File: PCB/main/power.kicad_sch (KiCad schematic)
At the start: 32 parts, among them IC4 FT230XS-R, IC5 MCP73831T-2ACI_OT, IC6 MCP1700T-3302E_TT, J10 PZ254V-11-02P, J5 47346-0001, J6 PZ254V-11-02P, J7 PZ254V-11-02P, J8 MTP125-1103S1, Q1 IRF9540NPbF

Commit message: new PCB
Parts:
- IC4: footprint SOP64P599X175-16N -> SamacSys_Parts_Power:SOP64P599X175-16N
- IC5: footprint SOT95P270X145-5N -> SamacSys_Parts_Power:SOT95P270X145-5N
- IC6: footprint SOT95P237X112-3N -> SamacSys_Parts_Power:SOT95P237X112-3N
- J10: footprint HDRV2W64P0X254_1X2_508X250X873P -> SamacSys_Parts_Power:HDRV2W64P0X254_1X2_508X250X873P
- J5: footprint SamacSys_Parts_Power:47346-0001 -> SamacSys_Parts_Microcontroller:47346-0001
- J6, J7: footprint SamacSys_Parts:HDRV2W64P0X254_1X2_508X250X873P -> SamacSys_Parts_Power:HDRV2W64P0X254_1X2_508X250X873P
- J8: footprint SamacSys_Parts:HDRV3W64P0X254_1X3_762X250X885P -> SamacSys_Parts_Power:HDRV3W64P0X254_1X3_762X250X885P
- TP1, TP2, TP3, TP4: footprint SamacSys_Parts:5017 -> SamacSys_Parts_Power:5017
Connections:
- net USART1_TX renamed PA9
- net USATR1_RX renamed PA10
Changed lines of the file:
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@@
+    (stroke (width 0) (type default) (color 0 0 0 0))
+  )
+  (wire (pts (xy 111.76 149.86) (xy 116.84 149.86))
     (stroke (width 0) (type default) (color 0 0 0 0))
   )
@@
   )
   (wire (pts (xy 175.26 161.29) (xy 175.26 163.83))
+    (stroke (width 0) (type default) (color 0 0 0 0))
+  )
+  (wire (pts (xy 111.76 157.48) (xy 116.84 157.48))
     (stroke (width 0) (type default) (color 0 0 0 0))
   )
@@
     (effects (font (size 1.27 1.27)) (justify left bottom))
   )
-  (label "RXD" (at 116.84 157.48 0)
+  (label "RXD" (at 111.76 157.48 0)
     (effects (font (size 1.27 1.27)) (justify left bottom))
   )
@@
     (effects (font (size 1.27 1.27)) (justify left bottom))
   )
-  (label "TXD" (at 116.84 149.86 0)
+  (label "TXD" (at 111.76 149.86 0)
     (effects (font (size 1.27 1.27)) (justify left bottom))
   )
+  (label "PA10" (at 172.72 144.78 0)
+    (effects (font (size 1.27 1.27)) (justify left bottom))
+  )
   (label "D-" (at 110.49 71.12 0)
+    (effects (font (size 1.27 1.27)) (justify left bottom))
+  )
+  (label "PA9" (at 172.72 142.24 0)
     (effects (font (size 1.27 1.27)) (justify left bottom))
   )
@@
     )
   )
-  (global_label "USART1_TX" (shape input) (at 172.72 142.24 0) (fields_autoplaced)
-    (effects (font (size 1.27 1.27)) (justify left))
-    (property "Intersheet References" "${INTERSHEET_REFS}" (id 0) (at 185.2647 142.1606 0)
-      (effects (font (size 1.27 1.27)) (justify left) hide)
-    )
-  )
   (global_label "VCC" (shape input) (at 212.09 96.52 90) (fields_autoplaced)
     (effects (font (size 1.27 1.27)) (justify left))
@@
     )
   )
-  (global_label "USATR1_RX" (shape input) (at 172.72 144.78 0) (fields_autoplaced)
-    (effects (font (size 1.27 1.27)) (justify left))
-    (property "Intersheet References" "${INTERSHEET_REFS}" (id 0) (at 185.5671 144.7006 0)
-      (effects (font (size 1.27 1.27)) (justify left) hide)
-    )
-  )
   (global_label "VCC" (shape input) (at 153.035 135.89 0) (fields_autoplaced)
     (effects (font (size 1.27 1.27)) (justify left))
@@
       (effects (font (size 1.27 1.27)) (justify right))
     )
-    (property "Footprint" "SamacSys_Parts:5017" (id 2) (at 119.38 52.07 0)
+    (property "Footprint" "SamacSys_Parts_Power:5017" (id 2) (at 119.38 52.07 0)
       (effects (font (size 1.27 1.27)) (justify left) hide)
     )
@@
       (effects (font (size 1.27 1.27)) (justify left))
     )
-    (property "Footprint" "SamacSys_Parts:HDRV2W64P0X254_1X2_508X250X873P" (id 2) (at 171.45 161.29 0)
+    (property "Footprint" "SamacSys_Parts_Power:HDRV2W64P0X254_1X2_508X250X873P" (id 2) (at 171.45 161.29 0)
       (effects (font (size 1.27 1.27)) (justify left) hide)
     )
@@
     (property "Reference" "IC5" (id 0) (at 134.62 93.98 0))
     (property "Value" "MCP73831T-2ACI_OT" (id 1) (at 134.62 96.52 0))
-    (property "Footprint" "SOT95P270X145-5N" (id 2) (at 124.46 109.22 0)
+    (property "Footprint" "SamacSys_Parts_Power:SOT95P270X145-5N" (id 2) (at 124.46 109.22 0)
       (effects (font (size 1.27 1.27)) (justify left) hide)
     )
@@
       (effects (font (size 1.27 1.27)) (justify left))
     )
-    (property "Footprint" "SamacSys_Parts:HDRV3W64P0X254_1X3_762X250X885P" (id 2) (at 217.17 118.11 0)
+    (property "Footprint" "SamacSys_Parts_Power:HDRV3W64P0X254_1X3_762X250X885P" (id 2) (at 217.17 118.11 0)
       (effects (font (size 1.27 1.27)) (justify left) hide)
     )
@@
       (effects (font (size 1.27 1.27)) (justify right))
     )
-    (property "Footprint" "SamacSys_Parts:5017" (id 2) (at 179.07 85.09 0)
+    (property "Footprint" "SamacSys_Parts_Power:5017" (id 2) (at 179.07 85.09 0)
       (effects (font (size 1.27 1.27)) (justify left) hide)
     )
@@
     (property "Reference" "J5" (id 0) (at 99.06 60.96 90))
     (property "Value" "47346-0001" (id 1) (at 99.06 63.5 90))
-    (property "Footprint" "SamacSys_Parts_Power:47346-0001" (id 2) (at 92.71 64.77 0)
+    (property "Footprint" "SamacSys_Parts_Microcontroller:47346-0001" (id 2) (at 92.71 64.77 0)
       (effects (font (size 1.27 1.27)) (justify left) hide)
     )
@@
     (property "Reference" "IC6" (id 0) (at 246.38 93.98 0))
     (property "Value" "MCP1700T-3302E_TT" (id 1) (at 246.38 96.52 0))
-    (property "Footprint" "SOT95P237X112-3N" (id 2) (at 236.22 106.68 0)
+    (property "Footprint" "SamacSys_Parts_Power:SOT95P237X112-3N" (id 2) (at 236.22 106.68 0)
       (effects (font (size 1.27 1.27)) (justify left) hide)
     )
@@
       (effects (font (size 1.27 1.27)) (justify right))
     )
-    (property "Footprint" "SamacSys_Parts:5017" (id 2) (at 265.43 85.09 0)
+    (property "Footprint" "SamacSys_Parts_Power:5017" (id 2) (at 265.43 85.09 0)
       (effects (font (size 1.27 1.27)) (justify left) hide)
     )
@@
       (effects (font (size 1.27 1.27)) (justify right))
     )
-    (property "Footprint" "SamacSys_Parts:5017" (id 2) (at 219.71 85.09 0)
+    (property "Footprint" "SamacSys_Parts_Power:5017" (id 2) (at 219.71 85.09 0)
       (effects (font (size 1.27 1.27)) (justify left) hide)
     )
@@
     (property "Reference" "IC4" (id 0) (at 133.35 142.24 0))
     (property "Value" "FT230XS-R" (id 1) (at 133.35 144.78 0))
-    (property "Footprint" "SOP64P599X175-16N" (id 2) (at 146.05 147.32 0)
+    (property "Footprint" "SamacSys_Parts_Power:SOP64P599X175-16N" (id 2) (at 146.05 147.32 0)
       (effects (font (size 1.27 1.27)) (justify left) hide)
     )
@@
       (effects (font (size 1.27 1.27)) (justify right))
     )
-    (property "Footprint" "SamacSys_Parts:HDRV2W64P0X254_1X2_508X250X873P" (id 2) (at 163.83 125.73 0)
+    (property "Footprint" "SamacSys_Parts_Power:HDRV2W64P0X254_1X2_508X250X873P" (id 2) (at 163.83 125.73 0)
       (effects (font (size 1.27 1.27)) (justify left) hide)
     )
@@
       (effects (font (size 1.27 1.27)) (justify left))
     )
-    (property "Footprint" "HDRV2W64P0X254_1X2_508X250X873P" (id 2) (at 191.77 109.22 0)
-      (effects (font (size 1.27 1.27)) (justify left) hide)
-    )
+    (property "Footprint" "SamacSys_Parts_Power:HDRV2W64P0X254_1X2_508X250X873P" (id 2) (at 191.77 109.22 0)
+      (effects (font (size 1.27 1.27)) (justify left) hide)
+    )

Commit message: generated Gerbers
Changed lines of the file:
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@@
   )
   (symbol (lib_id "SamacSys_Parts_power:PZ254V-11-02P") (at 168.91 144.78 270) (unit 1)
-    (in_bom yes) (on_board yes) (fields_autoplaced)
+    (in_bom yes) (on_board yes)
     (property "Reference" "J7" (id 0) (at 172.72 153.6699 90)
       (effects (font (size 1.27 1.27)) (justify left))
     )
-    (property "Value" "PZ254V-11-02P" (id 1) (at 172.72 156.2099 90)
+    (property "Value" "PZ254V-11-02P" (id 1) (at 154.94 154.94 90)
       (effects (font (size 1.27 1.27)) (justify left))
     )

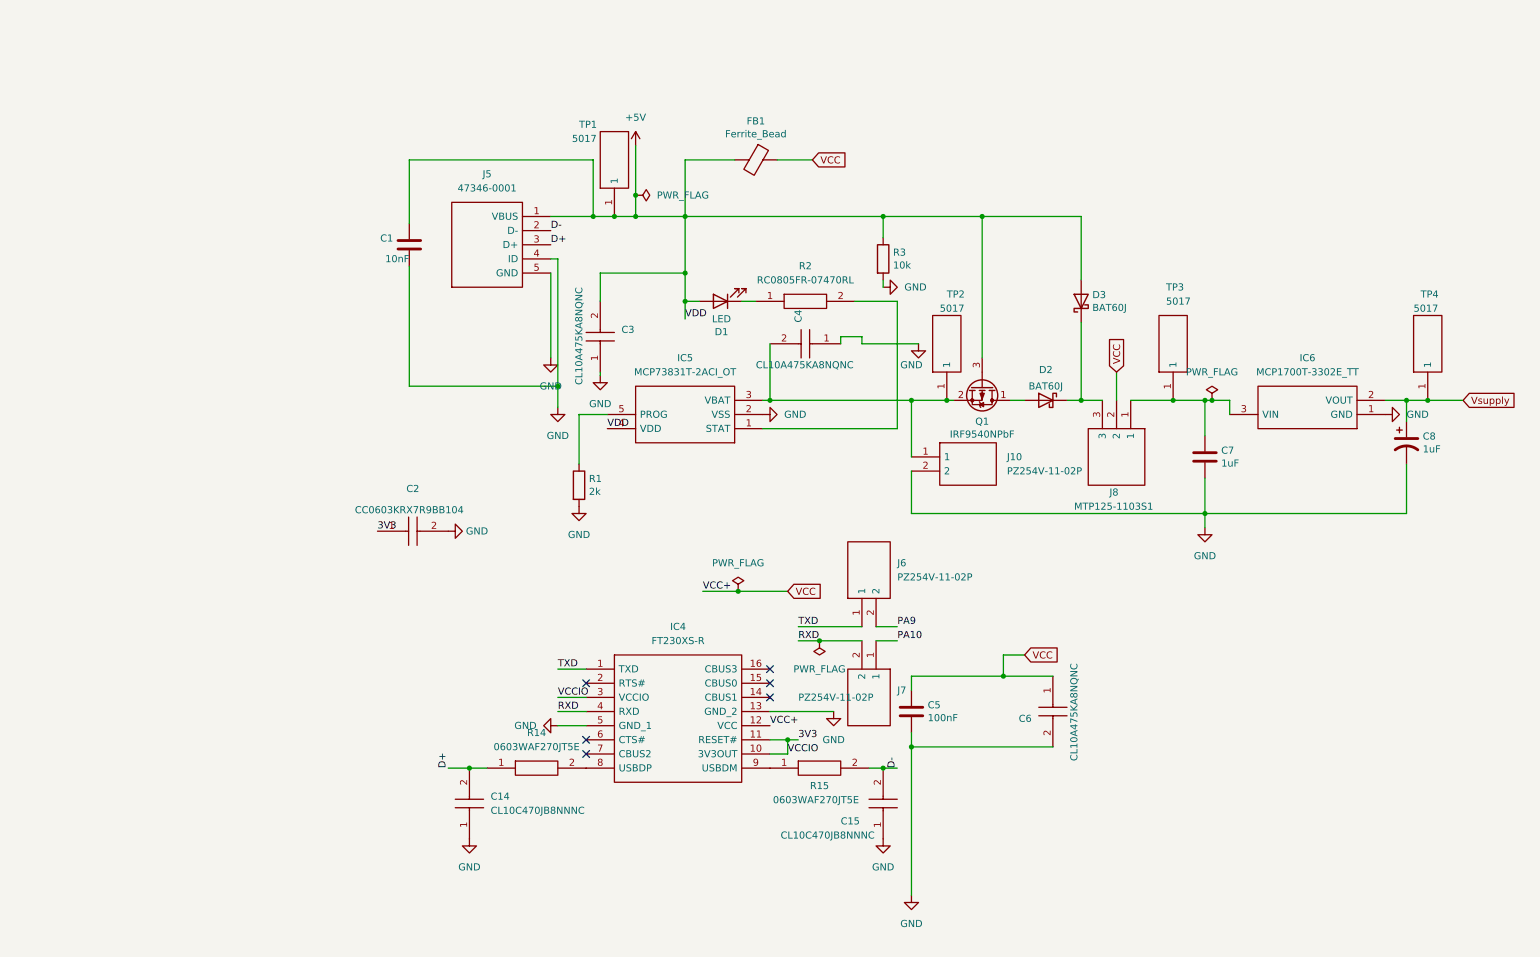
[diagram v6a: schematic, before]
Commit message: changed power schematic
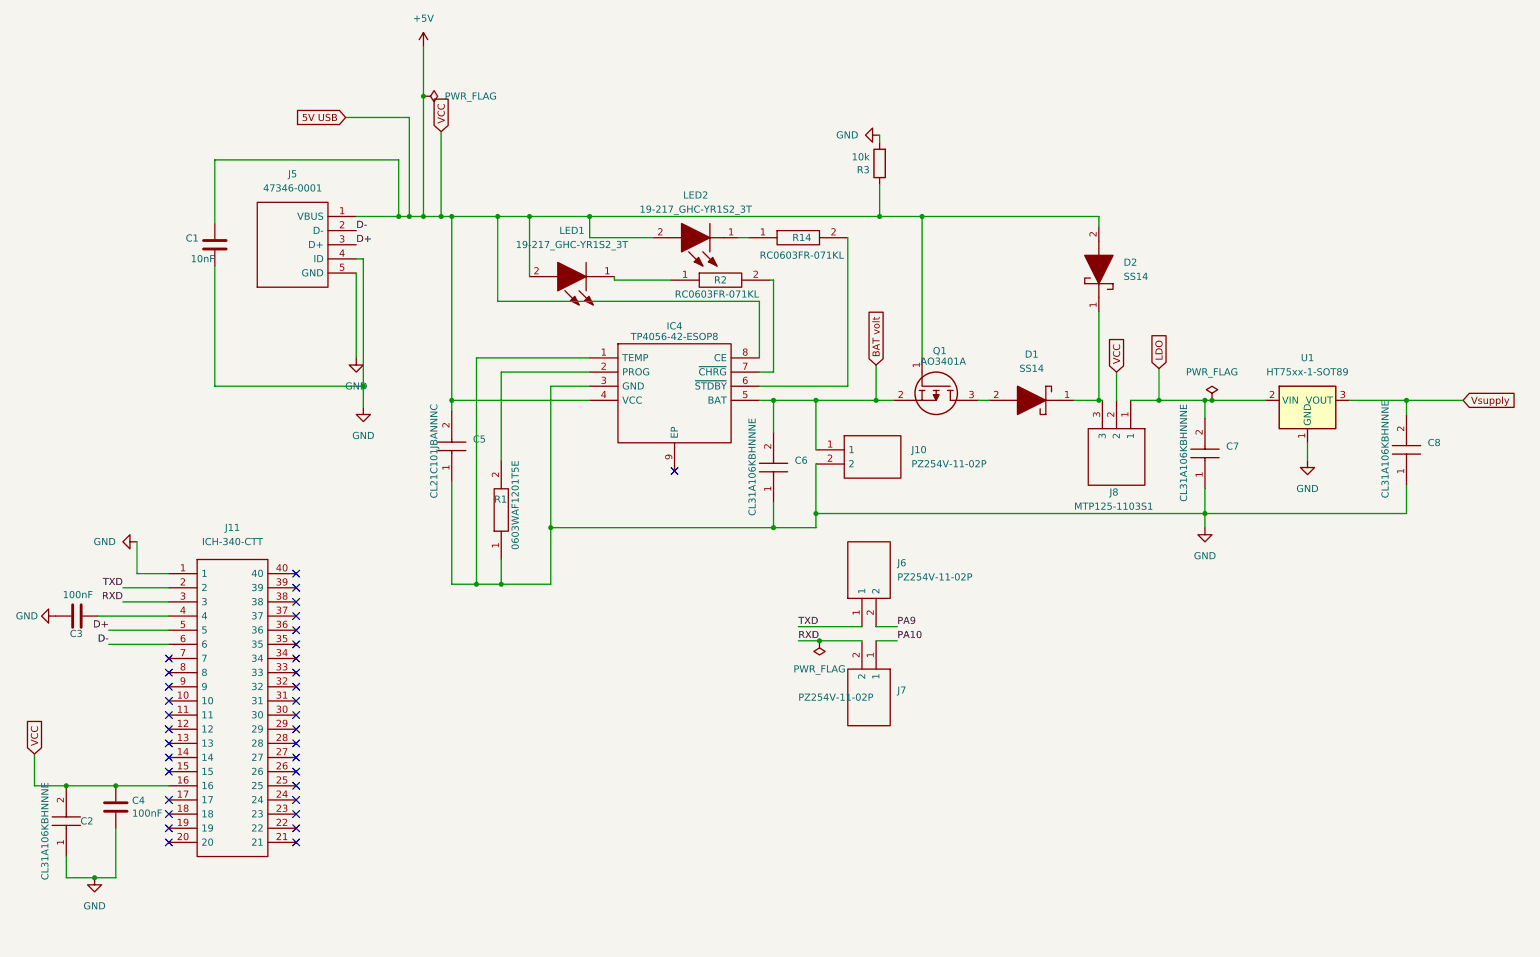
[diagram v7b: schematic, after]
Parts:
- removed C14, C15: CL10C470JB8NNNC, CAPC1608X90N, symbol SamacSys_Parts_power:CL10C470JB8NNNC
- removed C2: CC0603KRX7R9BB104, CAPC1608X90N, symbol SamacSys_Parts_power:CC0603KRX7R9BB104
- removed C3, C4, C6: CL10A475KA8NQNC, SamacSys_Parts_Microcontroller:CAPC1608X95N, symbol SamacSys_Parts_Microcontroller:CL10A475KA8NQNC
- removed C5: 100nF, SamacSys_Parts:CAPC1608X90N, symbol Device:C
- removed C7: 1uF, SamacSys_Parts:CAPC1608X90N, symbol Device:C
- removed C8: 1uF, SamacSys_Parts:CAPC1608X90N, symbol EEE3088_PROJECT-rescue:CP1-Device
- removed D1: LED, SamacSys_Parts:LEDC1608X70N, symbol Device:LED
- removed D2: BAT60J, Diode_SMD:D_SOD-323, symbol Device:D_Schottky
- removed D3: BAT60J, Diode_SMD:D_SOD-323, symbol Diode:BAT60A
- removed FB1: Ferrite_Bead, SamacSys_Parts:BEADC1608X95N, symbol EEE3088_PROJECT-rescue:Ferrite_Bead-Device
- removed IC4: FT230XS-R, SamacSys_Parts_Power:SOP64P599X175-16N, symbol SamacSys_Parts_power:FT230XS-R
- removed IC5: MCP73831T-2ACI_OT, SamacSys_Parts_Power:SOT95P270X145-5N, symbol SamacSys_Parts_power:MCP73831T-2ACI_OT
- removed IC6: MCP1700T-3302E_TT, SamacSys_Parts_Power:SOT95P237X112-3N, symbol SamacSys_Parts_power:MCP1700T-3302E_TT
- removed Q1: IRF9540NPbF, SamacSys_Parts_Power:TO254P469X1042X1967-3P, symbol Device:Q_PMOS_DSG
- removed R1: 2k, SamacSys_Parts:RESC1005X35N, symbol Device:R
- removed R14, R15: 0603WAF270JT5E, RESC1608X55N, symbol SamacSys_Parts_power:0603WAF270JT5E
- removed R2: RC0805FR-07470RL, SamacSys_Parts_Microcontroller:RESC2012X60N, symbol SamacSys_Parts_Microcontroller:RC0805FR-07470RL
- removed TP1, TP2, TP3, TP4: 5017, SamacSys_Parts_Power:5017, symbol SamacSys_Parts_power:5017
- added C2, C6, C7, C8: CL31A106KBHNNNE, SamacSys_Parts:CAPC3216X180N, symbol SamacSys_Parts_power:CL31A106KBHNNNE
- added C3, C4: 100nF, SamacSys_Parts:CAPC1608X90N, symbol Device:C
- added C5: CL21C101JBANNNC, SamacSys_Parts:CAPC2012X75N, symbol SamacSys_Parts_power:CL21C101JBANNNC
- added D1, D2: SS14, SamacSys_Parts:DIOM5227X270N, symbol SamacSys_Parts_power:SS14
- added IC4: TP4056-42-ESOP8, SamacSys_Parts:SOIC127P600X175-9N, symbol SamacSys_Parts_power:TP4056-42-ESOP8
- added J11: ICH-340-CTT, SamacSys_Parts:DIPS762W74P254L5080H338Q40N, symbol SamacSys_Parts_power:ICH-340-CTT
- added LED1, LED2: 19-217_GHC-YR1S2_3T, SamacSys_Parts:LEDC1608X50N, symbol SamacSys_Parts_power:19-217_GHC-YR1S2_3T
- added Q1: AO3401A, SamacSys_Parts:SOT95P280X125-3N, symbol SamacSys_Parts_power:AO3401A
- added R1: 0603WAF1201T5E, RESC1608X55N, symbol SamacSys_Parts_power:0603WAF1201T5E
- added R14, R2: RC0603FR-071KL, SamacSys_Parts:RESC1608X55N, symbol SamacSys_Parts_Microcontroller:RC0603FR-071KL
- added U1: HT75xx-1-SOT89, Package_TO_SOT_SMD:SOT-89-3, symbol Regulator_Linear:HT75xx-1-SOT89
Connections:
- net VCC is gone; now on net +5V: J8.2
- net +5V: now also C2.2, C4.1, C5.2, D2.2, IC4.4 (VCC), IC4.8 (CE), J11.16, LED1.2, LED2.2, Q1.1
- net D+: now also J11.5
- net D-: now also J11.6
- net GND: now also C2.1, C3.2, C4.2, C5.1, C6.1, C7.1, C8.1, IC4.1 (TEMP), IC4.3 (GND), J11.1, R1.1, U1.1 (GND)
- net RXD: now also J11.3
- net TXD: now also J11.2
- net Vsupply: now also C8.2, U1.3 (VOUT)
- net at J8.3: now also D1.1, D2.1
- net LDO: now reaches J8.1
- net LDO: now also C7.2, U1.2 (VIN)
- net BAT volt: now reaches J10.1
- net BAT volt: now also C6.2, IC4.5 (BAT), Q1.2
- new net: C3.1, J11.4
- new net: LED1.1, R2.1
- new net: IC4.7 (~{CHRG}), R2.2
- new net: LED2.1, R14.1
- new net: IC4.6 (~{STDBY}), R14.2
- new net: D1.2, Q1.3
- new net: IC4.2 (PROG), R1.2
- no-connect marks 6 -> 34
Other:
- moved on the sheet: C1, J10, J5, R3
